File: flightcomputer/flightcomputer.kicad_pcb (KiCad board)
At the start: 4 copper layers, 299 x 188 mm, 67 parts, among them J1 Conn_Coaxial, J10 Conn_01x03, J11 Conn_01x03, J12 M20-6102045, J2 Conn_Coaxial, J3 Conn_Coaxial, J4 Conn_Coaxial, J5 S3B-PH-K-S-GW, J6 S3B-PH-K-S-GW, J7 S4B-PH-K-S_LF__SN_, J8 S3B-PH-K-S-GW, J9 Conn_01x06, U1 MAX-M10S, U2 LIS2MDLTR, U3 BMI088, U4 MS5607-02BA, U7 Teensy4.1, U8 LSM6DSO32TR, U9 RFM96W-433S2

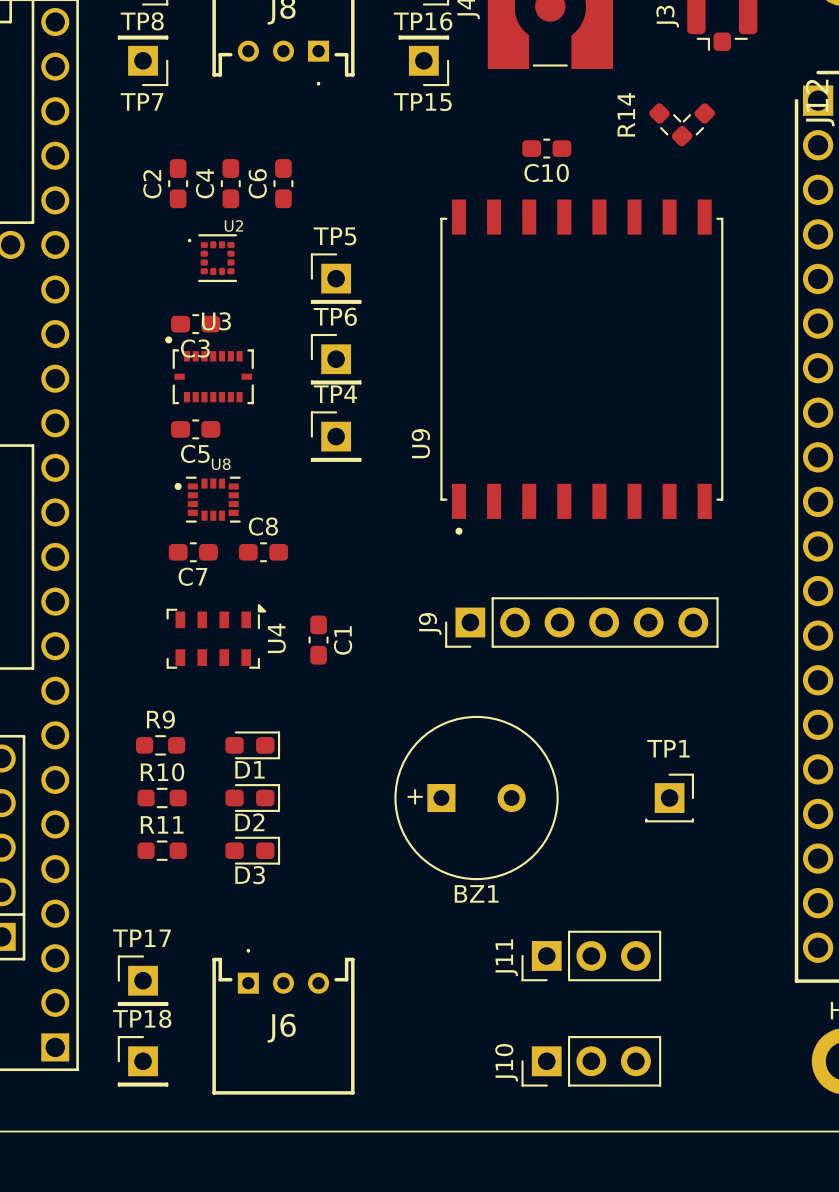
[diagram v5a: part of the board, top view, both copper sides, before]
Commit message: buck fixes and new components
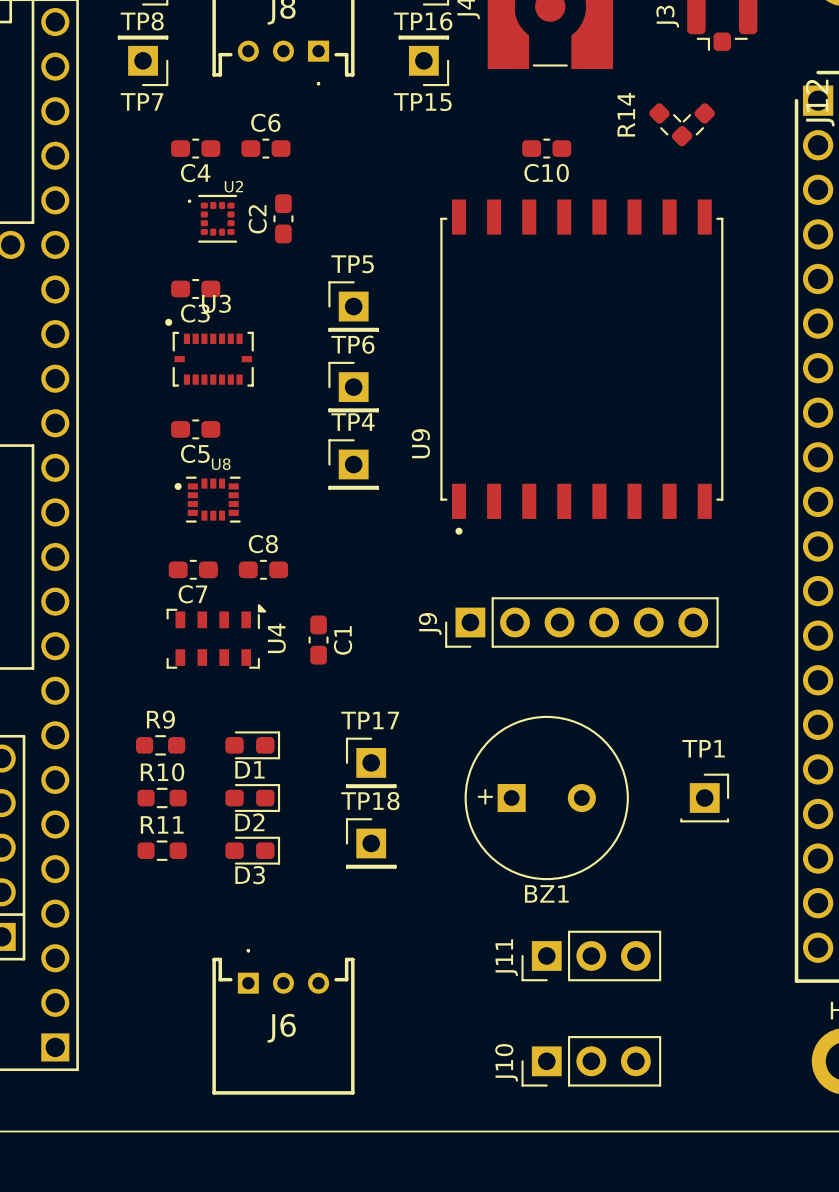
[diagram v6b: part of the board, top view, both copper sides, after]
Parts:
- moved TP17 18.0 mm to (112.0, 120.0)
- moved TP18 18.0 mm to (112.0, 124.6)
- moved C2 6.32 mm to (107.0, 89.0)
- moved BZ1 4.00 mm to (120.0, 122.0)
- moved C4 2.83 mm to (102.0, 85.0), turned to 180 degrees
- moved U2 2.24 mm to (103.2, 89.0)
- moved C6 2.24 mm to (106.0, 85.0), turned to 0 degrees
- moved C3 2.00 mm to (102.0, 93.0)
- moved TP1 2.00 mm to (131.0, 122.0)
- moved TP4 1.88 mm to (111.0, 103.0)
- moved TP5 1.88 mm to (111.0, 94.0)
- moved TP6 1.88 mm to (111.0, 98.6)
- moved C7 1.00 mm to (101.9, 109.0)
- moved C8 1.00 mm to (105.9, 109.0)
- moved U3 1.00 mm to (103.0, 97.0)
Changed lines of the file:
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@@
 	(footprint "Connector_PinHeader_2.54mm:PinHeader_1x01_P2.54mm_Vertical"
 		(layer "F.Cu")
-		(at 99 137)
+		(at 112 124.59)
 		(descr "Through hole straight pin header, 1x01, 2.54mm pitch, single row")
 		(tags "Through hole pin header THT 1x01 2.54mm single row")
@@
 	(footprint "Capacitor_SMD:C_0603_1608Metric_Pad1.08x0.95mm_HandSolder"
 		(layer "F.Cu")
-		(at 107 87 90)
+		(at 106 85)
 		(descr "Capacitor SMD 0603 (1608 Metric), square (rectangular) end terminal, IPC-7351 nominal with elongated pad for handsoldering. (Body size source: IPC-SM-782 page 76, https://www.pcb-3d.com/wordpress/wp-content/uploads/ipc-sm-782a_amendment_1_and_2.pdf), generated with kicad-footprint-generator")
 		(tags "capacitor handsolder")
 		(property "Reference" "C6"
-			(at 0 -1.43 90)
+			(at 0 -1.43 0)
 			(layer "F.SilkS")
 			(effects
@@
 		)
 		(property "Value" "10uF"
-			(at 0 1.43 90)
+			(at 0 1.43 0)
 			(layer "F.Fab")
 			(effects
@@
 		)
 		(property "Datasheet" "~"
-			(at 0 0 90)
+			(at 0 0 0)
 			(layer "F.Fab")
 			(hide yes)
@@
 		)
 		(property "Description" "Unpolarized capacitor, aluminum"
-			(at 0 0 90)
+			(at 0 0 0)
 			(layer "F.Fab")
 			(hide yes)
@@
 		)
 		(fp_line
-			(start 1.65 -0.73)
-			(end 1.65 0.73)
+			(start -1.65 -0.73)
+			(end 1.65 -0.73)
 			(stroke
 				(width 0.05)
@@
 		)
 		(fp_line
-			(start -1.65 -0.73)
-			(end 1.65 -0.73)
+			(start -1.65 0.73)
+			(end -1.65 -0.73)
 			(stroke
 				(width 0.05)
@@
 		)
 		(fp_line
-			(start 1.65 0.73)
-			(end -1.65 0.73)
+			(start 1.65 -0.73)
+			(end 1.65 0.73)
 			(stroke
 				(width 0.05)
@@
 		)
 		(fp_line
-			(start -1.65 0.73)
-			(end -1.65 -0.73)
+			(start 1.65 0.73)
+			(end -1.65 0.73)
 			(stroke
 				(width 0.05)
@@
 		)
 		(fp_line
-			(start 0.8 -0.4)
-			(end 0.8 0.4)
+			(start -0.8 -0.4)
+			(end 0.8 -0.4)
 			(stroke
 				(width 0.1)
@@
 		)
 		(fp_line
-			(start -0.8 -0.4)
-			(end 0.8 -0.4)
+			(start -0.8 0.4)
+			(end -0.8 -0.4)
 			(stroke
 				(width 0.1)
@@
 		)
 		(fp_line
-			(start 0.8 0.4)
-			(end -0.8 0.4)
+			(start 0.8 -0.4)
+			(end 0.8 0.4)
 			(stroke
 				(width 0.1)
@@
 		)
 		(fp_line
-			(start -0.8 0.4)
-			(end -0.8 -0.4)
+			(start 0.8 0.4)
+			(end -0.8 0.4)
 			(stroke
 				(width 0.1)
@@
 		)
 		(fp_text user "${REFERENCE}"
-			(at 0 0 90)
+			(at 0 0 0)
 			(layer "F.Fab")
 			(effects
@@
 		)
 		(pad "1" smd roundrect
-			(at -0.8625 0 90)
+			(at -0.8625 0)
 			(size 1.075 0.95)
 			(layers "F.Cu" "F.Mask" "F.Paste")
@@
 		)
 		(pad "2" smd roundrect
-			(at 0.8625 0 90)
+			(at 0.8625 0)
 			(size 1.075 0.95)
 			(layers "F.Cu" "F.Mask" "F.Paste")
@@
 	(footprint "Capacitor_SMD:C_0603_1608Metric_Pad1.08x0.95mm_HandSolder"
 		(layer "F.Cu")
-		(at 102 95 180)
+		(at 102 93 180)
 		(descr "Capacitor SMD 0603 (1608 Metric), square (rectangular) end terminal, IPC-7351 nominal with elongated pad for handsoldering. (Body size source: IPC-SM-782 page 76, https://www.pcb-3d.com/wordpress/wp-content/uploads/ipc-sm-782a_amendment_1_and_2.pdf), generated with kicad-footprint-generator")
 		(tags "capacitor handsolder")
@@
 	(footprint "Capacitor_SMD:C_0603_1608Metric_Pad1.08x0.95mm_HandSolder"
 		(layer "F.Cu")
-		(at 105.8625 108)
+		(at 105.8625 109)
 		(descr "Capacitor SMD 0603 (1608 Metric), square (rectangular) end terminal, IPC-7351 nominal with elongated pad for handsoldering. (Body size source: IPC-SM-782 page 76, https://www.pcb-3d.com/wordpress/wp-content/uploads/ipc-sm-782a_amendment_1_and_2.pdf), generated with kicad-footprint-generator")
 		(tags "capacitor handsolder")
@@
 	(footprint "Capacitor_SMD:C_0603_1608Metric_Pad1.08x0.95mm_HandSolder"
 		(layer "F.Cu")
-		(at 101 87 90)
+		(at 107 89 90)
 		(descr "Capacitor SMD 0603 (1608 Metric), square (rectangular) end terminal, IPC-7351 nominal with elongated pad for handsoldering. (Body size source: IPC-SM-782 page 76, https://www.pcb-3d.com/wordpress/wp-content/uploads/ipc-sm-782a_amendment_1_and_2.pdf), generated with kicad-footprint-generator")
 		(tags "capacitor handsolder")
@@
 	(footprint "Connector_PinHeader_2.54mm:PinHeader_1x01_P2.54mm_Vertical"
 		(layer "F.Cu")
-		(at 110 92.41)
+		(at 111 94)
 		(descr "Through hole straight pin header, 1x01, 2.54mm pitch, single row")
 		(tags "Through hole pin header THT 1x01 2.54mm single row")
@@
 	(footprint "Connector_PinHeader_2.54mm:PinHeader_1x01_P2.54mm_Vertical"
 		(layer "F.Cu")
-		(at 110 97)
+		(at 111 98.59)
 		(descr "Through hole straight pin header, 1x01, 2.54mm pitch, single row")
 		(tags "Through hole pin header THT 1x01 2.54mm single row")
@@
 	(footprint "Connector_PinHeader_2.54mm:PinHeader_1x01_P2.54mm_Vertical"
 		(layer "F.Cu")
-		(at 99 132.41)
+		(at 112 120)
 		(descr "Through hole straight pin header, 1x01, 2.54mm pitch, single row")
 		(tags "Through hole pin header THT 1x01 2.54mm single row")
@@
 	(footprint "HPRlibrary:PQFN50P200X200X70-12N"
 		(layer "F.Cu")
-		(at 103.25 91.24)
+		(at 103.25 89)
 		(property "Reference" "U2"
 			(at 0.932 -1.8064 0)
@@
 	(footprint "Buzzer_Beeper:MagneticBuzzer_PUI_AT-0927-TT-6-R"
 		(layer "F.Cu")
-		(at 116 122)
+		(at 120 122)
 		(descr "Buzzer Magnetic 9mm AT-0927-TT-6-R, http://www.puiaudio.com/pdf/AT-0927-TT-6-R.pdf")
 		(tags "Buzzer Magnetic 9mm AT-0927-TT-6-R")
@@
 	(footprint "Connector_PinHeader_2.54mm:PinHeader_1x01_P2.54mm_Vertical"
 		(layer "F.Cu")
-		(at 110 101.41)
+		(at 111 103)
 		(descr "Through hole straight pin header, 1x01, 2.54mm pitch, single row")
 		(tags "Through hole pin header THT 1x01 2.54mm single row")
@@
 	(footprint "HPRlibrary:PQFN50P450X300X100-16N"
 		(layer "F.Cu")
-		(at 103 98)
+		(at 103 97)
 		(property "Reference" "U3"
 			(at 0.178 -3.121 0)
@@
 	(footprint "Connector_PinSocket_2.54mm:PinSocket_1x01_P2.54mm_Vertical"
 		(layer "F.Cu")
-		(at 129 122)
+		(at 131 122)
 		(descr "Through hole straight socket strip, 1x01, 2.54mm pitch, single row (from Kicad 4.0.7), script generated")
 		(tags "Through hole socket strip THT 1x01 2.54mm single row")
@@
 	(footprint "Capacitor_SMD:C_0603_1608Metric_Pad1.08x0.95mm_HandSolder"
 		(layer "F.Cu")
-		(at 101.8625 108 180)
+		(at 101.8625 109 180)
 		(descr "Capacitor SMD 0603 (1608 Metric), square (rectangular) end terminal, IPC-7351 nominal with elongated pad for handsoldering. (Body size source: IPC-SM-782 page 76, https://www.pcb-3d.com/wordpress/wp-content/uploads/ipc-sm-782a_amendment_1_and_2.pdf), generated with kicad-footprint-generator")
 		(tags "capacitor handsolder")
@@
 	(footprint "Capacitor_SMD:C_0603_1608Metric_Pad1.08x0.95mm_HandSolder"
 		(layer "F.Cu")
-		(at 104 87 90)
+		(at 102 85 180)
 		(descr "Capacitor SMD 0603 (1608 Metric), square (rectangular) end terminal, IPC-7351 nominal with elongated pad for handsoldering. (Body size source: IPC-SM-782 page 76, https://www.pcb-3d.com/wordpress/wp-content/uploads/ipc-sm-782a_amendment_1_and_2.pdf), generated with kicad-footprint-generator")
 		(tags "capacitor handsolder")
 		(property "Reference" "C4"
-			(at 0 -1.43 90)
+			(at 0 -1.43 0)
 			(layer "F.SilkS")
 			(effects
@@
 		)
 		(property "Value" "100nF"
-			(at 0 1.43 90)
+			(at 0 1.43 0)
 			(layer "F.Fab")
 			(effects
@@
 		)
 		(property "Datasheet" "~"
-			(at 0 0 90)
+			(at 0 0 0)
 			(layer "F.Fab")
 			(hide yes)
@@
 		)
 		(property "Description" "Unpolarized capacitor, ceramic"
-			(at 0 0 90)
+			(at 0 0 0)
 			(layer "F.Fab")
 			(hide yes)
@@
 		(attr smd)
 		(fp_line
-			(start -0.146267 -0.51)
-			(end 0.146267 -0.51)
+			(start -0.146267 0.51)
+			(end 0.146267 0.51)
 			(stroke
 				(width 0.12)
@@
 		)
 		(fp_line
-			(start -0.146267 0.51)
-			(end 0.146267 0.51)
+			(start -0.146267 -0.51)
+			(end 0.146267 -0.51)
 			(stroke
 				(width 0.12)
@@
 		)
 		(fp_line
-			(start 1.65 -0.73)
-			(end 1.65 0.73)
+			(start 1.65 0.73)
+			(end -1.65 0.73)
 			(stroke
 				(width 0.05)
@@
 		)
 		(fp_line
-			(start -1.65 -0.73)
-			(end 1.65 -0.73)
+			(start 1.65 -0.73)
+			(end 1.65 0.73)
 			(stroke
 				(width 0.05)
@@
 		)
 		(fp_line
-			(start 1.65 0.73)
-			(end -1.65 0.73)
+			(start -1.65 0.73)
+			(end -1.65 -0.73)
 			(stroke
 				(width 0.05)
@@
 		)
 		(fp_line
-			(start -1.65 0.73)
-			(end -1.65 -0.73)
+			(start -1.65 -0.73)
+			(end 1.65 -0.73)
 			(stroke
 				(width 0.05)
@@
 		)
 		(fp_line
-			(start 0.8 -0.4)
-			(end 0.8 0.4)
+			(start 0.8 0.4)
+			(end -0.8 0.4)
 			(stroke
 				(width 0.1)
@@
 		)
 		(fp_line
-			(start -0.8 -0.4)
-			(end 0.8 -0.4)
+			(start 0.8 -0.4)
+			(end 0.8 0.4)
 			(stroke
 				(width 0.1)
@@
 		)
 		(fp_line
-			(start 0.8 0.4)
-			(end -0.8 0.4)
+			(start -0.8 0.4)
+			(end -0.8 -0.4)
 			(stroke
 				(width 0.1)
@@
 		)
 		(fp_line
-			(start -0.8 0.4)
-			(end -0.8 -0.4)
+			(start -0.8 -0.4)
+			(end 0.8 -0.4)
 			(stroke
 				(width 0.1)
@@
 		)
 		(fp_text user "${REFERENCE}"
-			(at 0 0 90)
+			(at 0 0 0)
 			(layer "F.Fab")
 			(effects
@@
 		)
 		(pad "1" smd roundrect
-			(at -0.8625 0 90)
+			(at -0.8625 0 180)
 			(size 1.075 0.95)
 			(layers "F.Cu" "F.Mask" "F.Paste")
@@
 		)
 		(pad "2" smd roundrect
-			(at 0.8625 0 90)
+			(at 0.8625 0 180)
 			(size 1.075 0.95)
 			(layers "F.Cu" "F.Mask" "F.Paste")

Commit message: nuked placement, will update
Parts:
- moved J11 75.7 mm to (66.9, 79.0)
- moved J4 52.7 mm to (130.0, 129.0), turned to 180 degrees
- moved C10 51.1 mm to (148.0, 129.0)
- moved J9 45.7 mm to (162.0, 123.1), turned to 180 degrees
- moved R14 42.0 mm to (136.2, 124.1), turned to 180 degrees
- moved J3 41.4 mm to (130.9, 119.2), turned to 180 degrees
- moved J12 40.7 mm to (177.5, 74.5)
- moved U9 32.8 mm to (150.0, 117.0), turned to -90 degrees
- moved TP1 24.8 mm to (147.0, 103.0)
- moved H2 21.8 mm to (160.0, 69.0)
- moved H3 21.8 mm to (160.0, 131.0)
- moved J10 21.8 mm to (101.0, 131.0), turned to 180 degrees
- moved R17 20.3 mm to (41.1, 100.5)
- moved S1 20.3 mm to (41.0, 108.5)
- moved H1 19.0 mm to (43.0, 69.0)
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
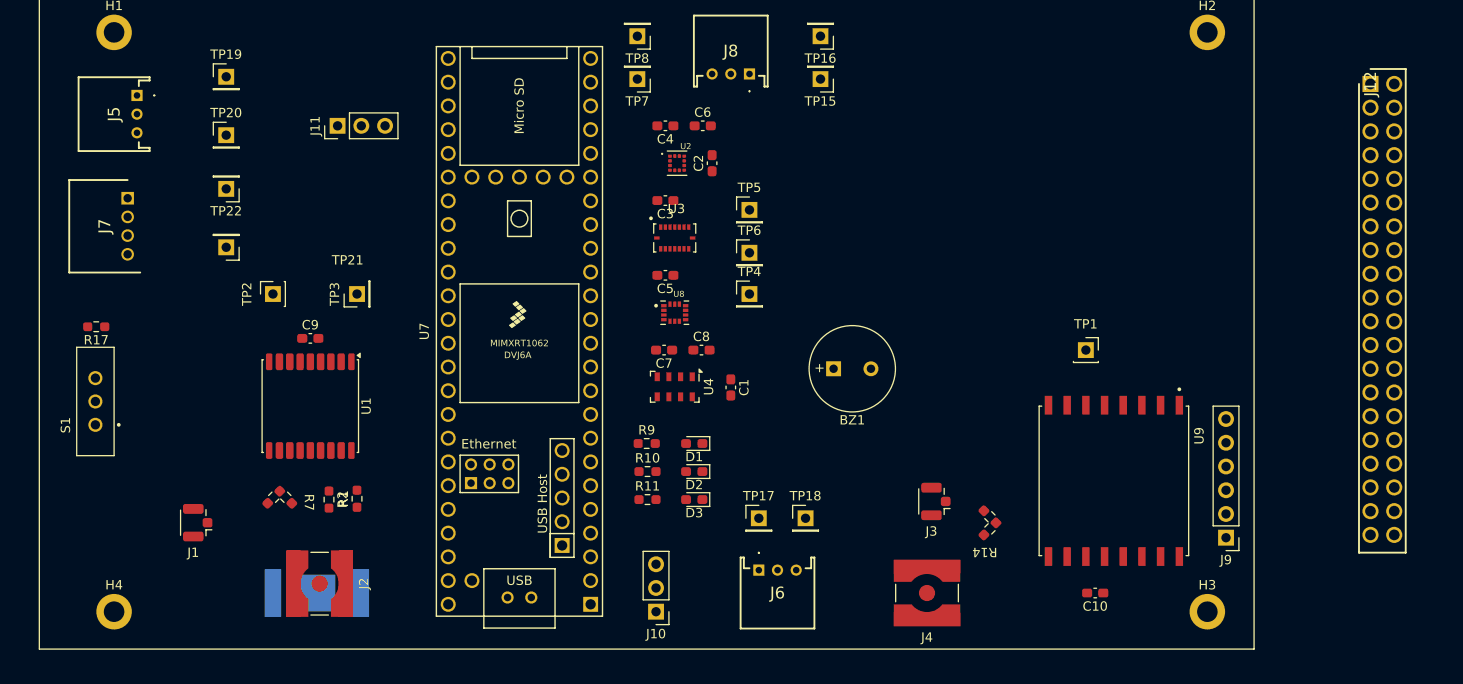
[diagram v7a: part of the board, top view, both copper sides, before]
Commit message: connector nets
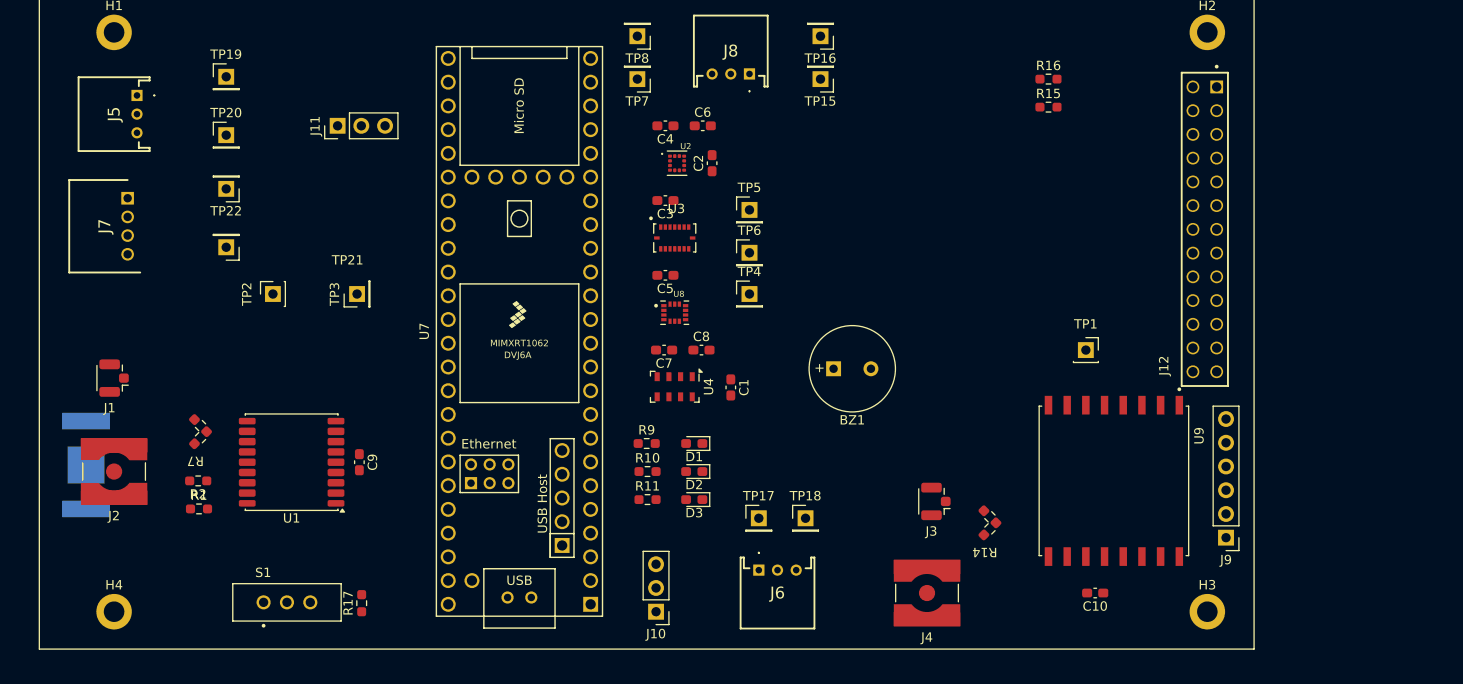
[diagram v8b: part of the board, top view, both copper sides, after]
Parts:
- added R15: 0, Resistor_SMD:R_0603_1608Metric_Pad0.98x0.95mm_HandSolder, F.Cu at (143.0, 77.0)
- added R16: 0, Resistor_SMD:R_0603_1608Metric_Pad0.98x0.95mm_HandSolder, F.Cu at (143.0, 74.0)
- J12: value M20-6102045 -> ESQ-113-14-G-D; footprint HPRlibrary:RHDR40W66P254_2X20_5146X500X1105P -> HPRlibrary:SAMTEC_ESQ-113-14-G-D
- moved R17 41.0 mm to (69.5, 130.1), turned to 90 degrees
- moved S1 29.7 mm to (61.5, 130.0), turned to 0 degrees
- moved BT1 28.2 mm to (40.0, 115.3), turned to 90 degrees
- moved J2 25.1 mm to (43.0, 116.0), turned to 180 degrees
- moved J1 17.9 mm to (43.0, 106.0)
- moved R1 16.9 mm to (52.1, 120.0), turned to 0 degrees
- moved J12 16.5 mm to (161.0, 74.8), turned to 90 degrees
- moved C9 14.3 mm to (69.2, 115.0), turned to -90 degrees
- moved R2 14.1 mm to (52.0, 117.0), turned to 180 degrees
- moved R7 12.7 mm to (51.7, 114.4), turned to 180 degrees
- moved U1 6.32 mm to (62.0, 115.0), turned to 180 degrees
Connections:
- J12 pad 10: unconnected-(J12-Pad10) -> /5V
- J12 pad 11: unconnected-(J12-Pad11) -> /can_tx
- J12 pad 12: unconnected-(J12-Pad12) -> /5V
- J12 pad 13: unconnected-(J12-Pad13) -> /SENSE_mosi
- J12 pad 14: unconnected-(J12-Pad14) -> /5V
- J12 pad 15: unconnected-(J12-Pad15) -> /SENSE_miso
- J12 pad 16: unconnected-(J12-Pad16) -> GND
- J12 pad 17: unconnected-(J12-Pad17) -> /SENSE_sck
- J12 pad 18: unconnected-(J12-Pad18) -> GND
- J12 pad 19: unconnected-(J12-Pad19) -> /servo2_pwm
- J12 pad 20: unconnected-(J12-Pad20) -> GND
- J12 pad 21: unconnected-(J12-Pad21) -> /servo1_pwm
- J12 pad 22: unconnected-(J12-Pad22) -> GND
- J12 pad 23: unconnected-(J12-Pad23) -> /PYRO1
- J12 pad 24: unconnected-(J12-Pad24) -> GND
- J12 pad 25: unconnected-(J12-Pad25) -> /PYRO2
- J12 pad 26: unconnected-(J12-Pad26) -> GND
